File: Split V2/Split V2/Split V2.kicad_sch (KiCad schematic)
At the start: 60 parts

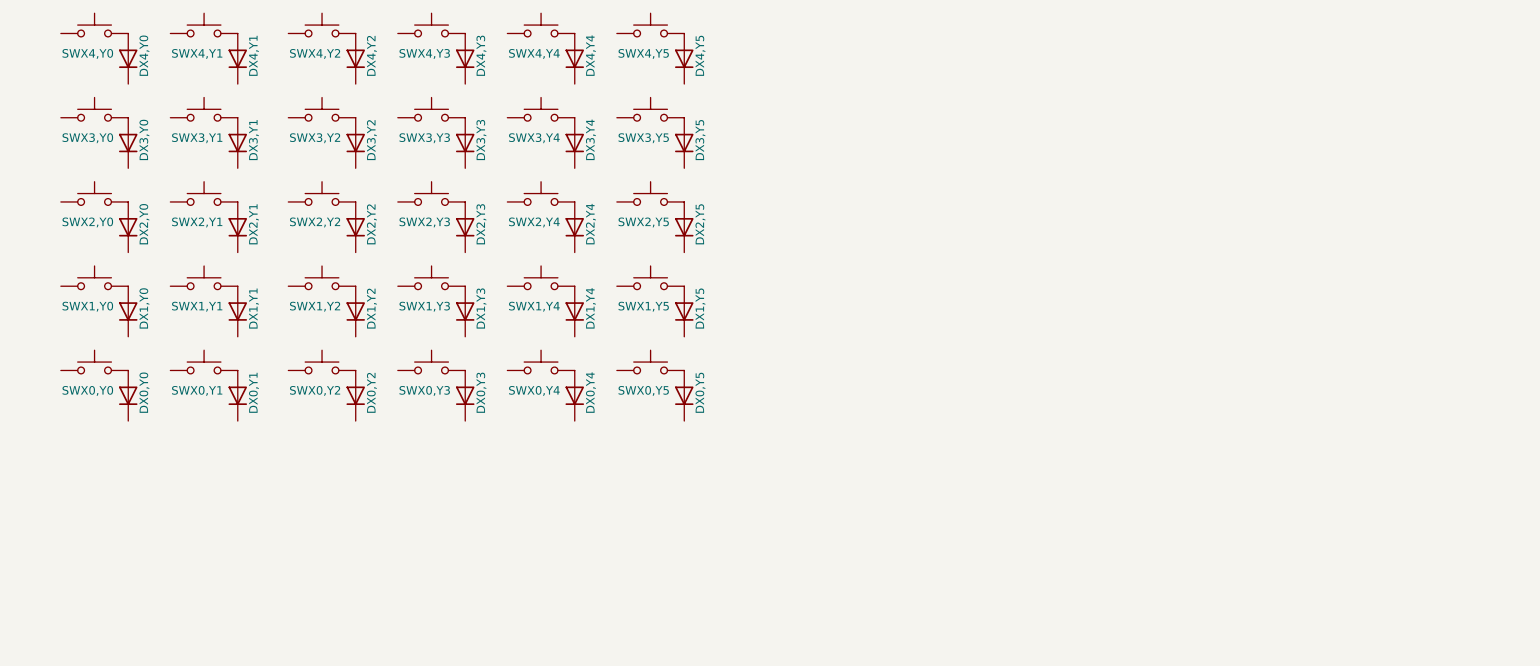
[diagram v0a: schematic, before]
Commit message: Connected schematic and pcb
Got the Schematic and pcb linked and started searching for symbols for arduio promicro
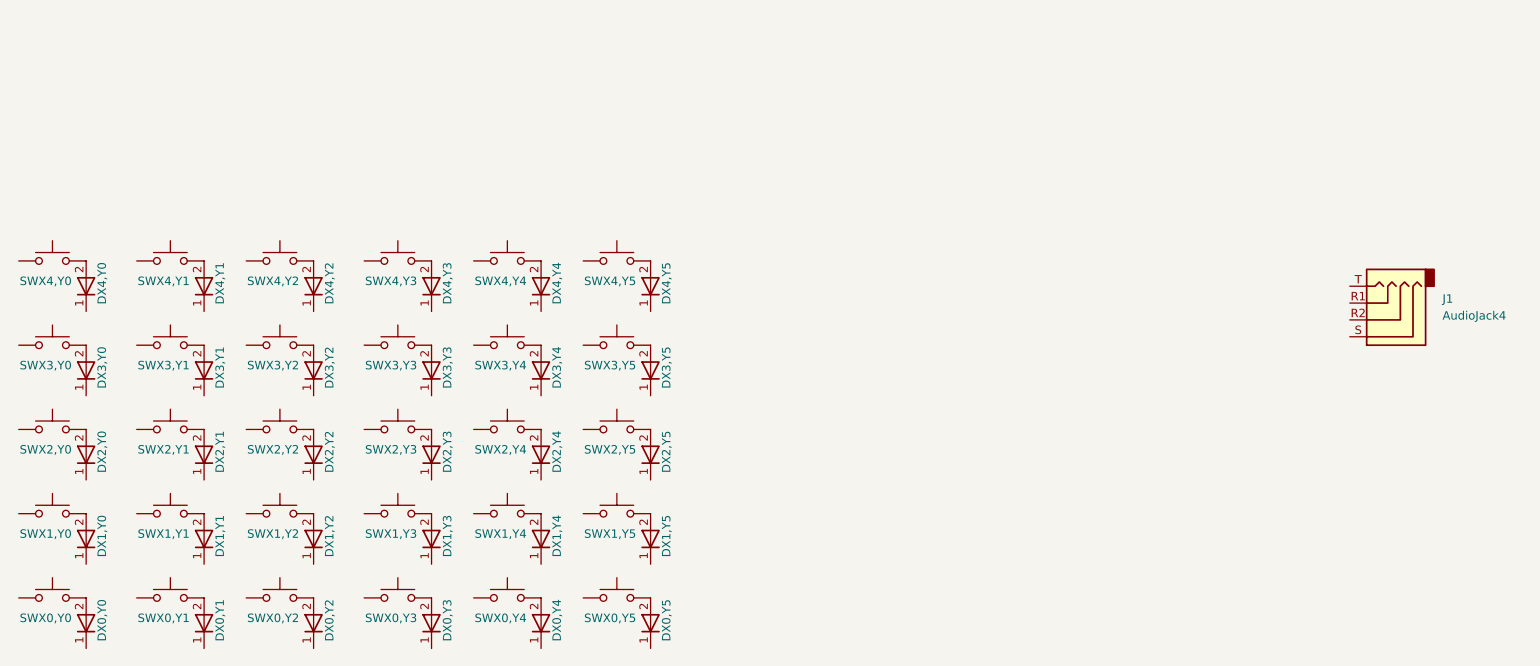
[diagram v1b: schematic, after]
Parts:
- removed DX0,Y5, DX1,Y5, DX2,Y5, DX3,Y5, DX4,Y5: BAV16W, Diode_SMD:D_SOD-123, symbol Diode:BAV16W
- removed SWX0,Y5, SWX1,Y5, SWX2,Y5, SWX3,Y5, SWX4,Y5: SW_Push, symbol Switch:SW_Push
- added DX0,Y0, DX1,Y0, DX2,Y0, DX3,Y0, DX4,Y0: ~, Custom:D_SOD-123_bothside, symbol Simulation_SPICE:D
- added J1: AudioJack4, symbol Connector_Audio:AudioJack4
- added SWX0,Y0, SWX1,Y0, SWX2,Y0, SWX3,Y0, SWX4,Y0: ~, keyswitches.pretty-master:Kailh_socket_PG1350_optional_reversible, symbol Switch:SW_Push
- DX0,Y1: renamed from DX0,Y0; value BAV16W -> ~; footprint Diode_SMD:D_SOD-123 -> Custom:D_SOD-123_bothside; symbol Diode:BAV16W -> Simulation_SPICE:D
- DX0,Y2: renamed from DX0,Y1; value BAV16W -> ~; footprint Diode_SMD:D_SOD-123 -> Custom:D_SOD-123_bothside; symbol Diode:BAV16W -> Simulation_SPICE:D
- DX0,Y3: renamed from DX0,Y2; value BAV16W -> ~; footprint Diode_SMD:D_SOD-123 -> Custom:D_SOD-123_bothside; symbol Diode:BAV16W -> Simulation_SPICE:D
- DX0,Y4: renamed from DX0,Y3; value BAV16W -> ~; footprint Diode_SMD:D_SOD-123 -> Custom:D_SOD-123_bothside; symbol Diode:BAV16W -> Simulation_SPICE:D
- DX0,Y5: renamed from DX0,Y4; value BAV16W -> ~; footprint Diode_SMD:D_SOD-123 -> Custom:D_SOD-123_bothside; symbol Diode:BAV16W -> Simulation_SPICE:D
- DX1,Y1: renamed from DX1,Y0; value BAV16W -> ~; footprint Diode_SMD:D_SOD-123 -> Custom:D_SOD-123_bothside; symbol Diode:BAV16W -> Simulation_SPICE:D
- DX1,Y2: renamed from DX1,Y1; value BAV16W -> ~; footprint Diode_SMD:D_SOD-123 -> Custom:D_SOD-123_bothside; symbol Diode:BAV16W -> Simulation_SPICE:D
- DX1,Y3: renamed from DX1,Y2; value BAV16W -> ~; footprint Diode_SMD:D_SOD-123 -> Custom:D_SOD-123_bothside; symbol Diode:BAV16W -> Simulation_SPICE:D
- DX1,Y4: renamed from DX1,Y3; value BAV16W -> ~; footprint Diode_SMD:D_SOD-123 -> Custom:D_SOD-123_bothside; symbol Diode:BAV16W -> Simulation_SPICE:D
- DX1,Y5: renamed from DX1,Y4; value BAV16W -> ~; footprint Diode_SMD:D_SOD-123 -> Custom:D_SOD-123_bothside; symbol Diode:BAV16W -> Simulation_SPICE:D
- DX2,Y1: renamed from DX2,Y0; value BAV16W -> ~; footprint Diode_SMD:D_SOD-123 -> Custom:D_SOD-123_bothside; symbol Diode:BAV16W -> Simulation_SPICE:D
- DX2,Y2: renamed from DX2,Y1; value BAV16W -> ~; footprint Diode_SMD:D_SOD-123 -> Custom:D_SOD-123_bothside; symbol Diode:BAV16W -> Simulation_SPICE:D
- DX2,Y3: renamed from DX2,Y2; value BAV16W -> ~; footprint Diode_SMD:D_SOD-123 -> Custom:D_SOD-123_bothside; symbol Diode:BAV16W -> Simulation_SPICE:D
- DX2,Y4: renamed from DX2,Y3; value BAV16W -> ~; footprint Diode_SMD:D_SOD-123 -> Custom:D_SOD-123_bothside; symbol Diode:BAV16W -> Simulation_SPICE:D
- DX2,Y5: renamed from DX2,Y4; value BAV16W -> ~; footprint Diode_SMD:D_SOD-123 -> Custom:D_SOD-123_bothside; symbol Diode:BAV16W -> Simulation_SPICE:D
- DX3,Y1: renamed from DX3,Y0; value BAV16W -> ~; footprint Diode_SMD:D_SOD-123 -> Custom:D_SOD-123_bothside; symbol Diode:BAV16W -> Simulation_SPICE:D
- DX3,Y2: renamed from DX3,Y1; value BAV16W -> ~; footprint Diode_SMD:D_SOD-123 -> Custom:D_SOD-123_bothside; symbol Diode:BAV16W -> Simulation_SPICE:D
- DX3,Y3: renamed from DX3,Y2; value BAV16W -> ~; footprint Diode_SMD:D_SOD-123 -> Custom:D_SOD-123_bothside; symbol Diode:BAV16W -> Simulation_SPICE:D
- DX3,Y4: renamed from DX3,Y3; value BAV16W -> ~; footprint Diode_SMD:D_SOD-123 -> Custom:D_SOD-123_bothside; symbol Diode:BAV16W -> Simulation_SPICE:D
- DX3,Y5: renamed from DX3,Y4; value BAV16W -> ~; footprint Diode_SMD:D_SOD-123 -> Custom:D_SOD-123_bothside; symbol Diode:BAV16W -> Simulation_SPICE:D
- DX4,Y1: renamed from DX4,Y0; value BAV16W -> ~; footprint Diode_SMD:D_SOD-123 -> Custom:D_SOD-123_bothside; symbol Diode:BAV16W -> Simulation_SPICE:D
- DX4,Y2: renamed from DX4,Y1; value BAV16W -> ~; footprint Diode_SMD:D_SOD-123 -> Custom:D_SOD-123_bothside; symbol Diode:BAV16W -> Simulation_SPICE:D
- DX4,Y3: renamed from DX4,Y2; value BAV16W -> ~; footprint Diode_SMD:D_SOD-123 -> Custom:D_SOD-123_bothside; symbol Diode:BAV16W -> Simulation_SPICE:D
- DX4,Y4: renamed from DX4,Y3; value BAV16W -> ~; footprint Diode_SMD:D_SOD-123 -> Custom:D_SOD-123_bothside; symbol Diode:BAV16W -> Simulation_SPICE:D
- DX4,Y5: renamed from DX4,Y4; value BAV16W -> ~; footprint Diode_SMD:D_SOD-123 -> Custom:D_SOD-123_bothside; symbol Diode:BAV16W -> Simulation_SPICE:D
- SWX0,Y1: renamed from SWX0,Y0; value SW_Push -> ~; footprint (none) -> keyswitches.pretty-master:Kailh_socket_PG1350_optional_reversible
- SWX0,Y2: renamed from SWX0,Y1; value SW_Push -> ~; footprint (none) -> keyswitches.pretty-master:Kailh_socket_PG1350_optional_reversible
- SWX0,Y3: renamed from SWX0,Y2; value SW_Push -> ~; footprint (none) -> keyswitches.pretty-master:Kailh_socket_PG1350_optional_reversible
- SWX0,Y4: renamed from SWX0,Y3; value SW_Push -> ~; footprint (none) -> keyswitches.pretty-master:Kailh_socket_PG1350_optional_reversible
- SWX0,Y5: renamed from SWX0,Y4; value SW_Push -> ~; footprint (none) -> keyswitches.pretty-master:Kailh_socket_PG1350_optional_reversible
- SWX1,Y1: renamed from SWX1,Y0; value SW_Push -> ~; footprint (none) -> keyswitches.pretty-master:Kailh_socket_PG1350_optional_reversible
- SWX1,Y2: renamed from SWX1,Y1; value SW_Push -> ~; footprint (none) -> keyswitches.pretty-master:Kailh_socket_PG1350_optional_reversible
- SWX1,Y3: renamed from SWX1,Y2; value SW_Push -> ~; footprint (none) -> keyswitches.pretty-master:Kailh_socket_PG1350_optional_reversible
- SWX1,Y4: renamed from SWX1,Y3; value SW_Push -> ~; footprint (none) -> keyswitches.pretty-master:Kailh_socket_PG1350_optional_reversible
- SWX1,Y5: renamed from SWX1,Y4; value SW_Push -> ~; footprint (none) -> keyswitches.pretty-master:Kailh_socket_PG1350_optional_reversible
- SWX2,Y1: renamed from SWX2,Y0; value SW_Push -> ~; footprint (none) -> keyswitches.pretty-master:Kailh_socket_PG1350_optional_reversible
- SWX2,Y2: renamed from SWX2,Y1; value SW_Push -> ~; footprint (none) -> keyswitches.pretty-master:Kailh_socket_PG1350_optional_reversible
- SWX2,Y3: renamed from SWX2,Y2; value SW_Push -> ~; footprint (none) -> keyswitches.pretty-master:Kailh_socket_PG1350_optional_reversible
- SWX2,Y4: renamed from SWX2,Y3; value SW_Push -> ~; footprint (none) -> keyswitches.pretty-master:Kailh_socket_PG1350_optional_reversible
- SWX2,Y5: renamed from SWX2,Y4; value SW_Push -> ~; footprint (none) -> keyswitches.pretty-master:Kailh_socket_PG1350_optional_reversible
- SWX3,Y1: renamed from SWX3,Y0; value SW_Push -> ~; footprint (none) -> keyswitches.pretty-master:Kailh_socket_PG1350_optional_reversible
- SWX3,Y2: renamed from SWX3,Y1; value SW_Push -> ~; footprint (none) -> keyswitches.pretty-master:Kailh_socket_PG1350_optional_reversible
- SWX3,Y3: renamed from SWX3,Y2; value SW_Push -> ~; footprint (none) -> keyswitches.pretty-master:Kailh_socket_PG1350_optional_reversible
- SWX3,Y4: renamed from SWX3,Y3; value SW_Push -> ~; footprint (none) -> keyswitches.pretty-master:Kailh_socket_PG1350_optional_reversible
- SWX3,Y5: renamed from SWX3,Y4; value SW_Push -> ~; footprint (none) -> keyswitches.pretty-master:Kailh_socket_PG1350_optional_reversible
- SWX4,Y1: renamed from SWX4,Y0; value SW_Push -> ~; footprint (none) -> keyswitches.pretty-master:Kailh_socket_PG1350_optional_reversible
- SWX4,Y2: renamed from SWX4,Y1; value SW_Push -> ~; footprint (none) -> keyswitches.pretty-master:Kailh_socket_PG1350_optional_reversible
- SWX4,Y3: renamed from SWX4,Y2; value SW_Push -> ~; footprint (none) -> keyswitches.pretty-master:Kailh_socket_PG1350_optional_reversible
- SWX4,Y4: renamed from SWX4,Y3; value SW_Push -> ~; footprint (none) -> keyswitches.pretty-master:Kailh_socket_PG1350_optional_reversible
- SWX4,Y5: renamed from SWX4,Y4; value SW_Push -> ~; footprint (none) -> keyswitches.pretty-master:Kailh_socket_PG1350_optional_reversible
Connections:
- new net: DX4,Y0.2 (A), SWX4,Y0.2
- new net: DX2,Y0.2 (A), SWX2,Y0.2
- new net: DX0,Y0.2 (A), SWX0,Y0.2
- new net: DX3,Y0.2 (A), SWX3,Y0.2
- new net: DX1,Y0.2 (A), SWX1,Y0.2
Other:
- moved on the sheet: SWX0,Y1, SWX0,Y2, SWX0,Y3, SWX0,Y4, SWX0,Y5, SWX1,Y1, SWX1,Y2, SWX1,Y3, SWX1,Y4, SWX1,Y5, SWX2,Y1, SWX2,Y2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
